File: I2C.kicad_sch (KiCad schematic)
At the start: 12 parts, among them U10 TCA9548AMRGER

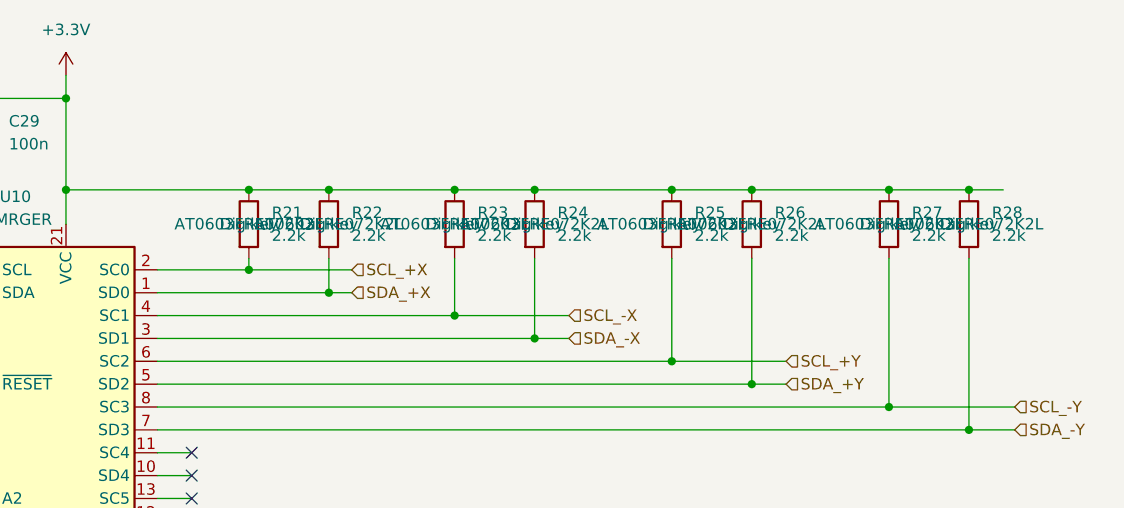
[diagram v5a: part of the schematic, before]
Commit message: Small schematic changes
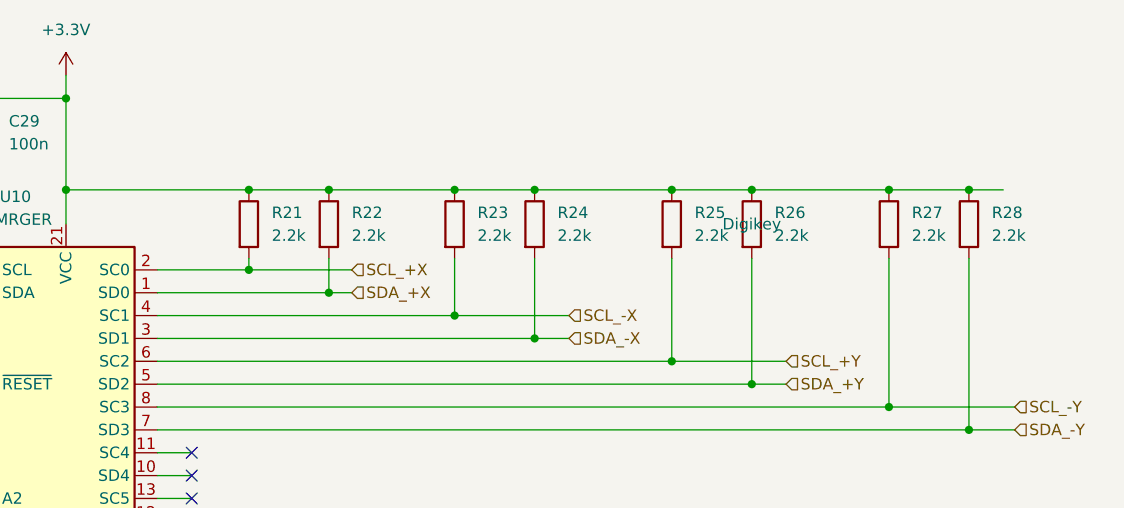
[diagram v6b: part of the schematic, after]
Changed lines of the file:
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@@
 					(size 1.27 1.27)
 				)
+				(hide yes)
 			)
 		)
@@
 					(size 1.27 1.27)
 				)
+				(hide yes)
 			)
 		)
@@
 					(size 1.27 1.27)
 				)
+				(hide yes)
 			)
 		)
@@
 					(size 1.27 1.27)
 				)
+				(hide yes)
 			)
 		)
@@
 					(size 1.27 1.27)
 				)
+				(hide yes)
 			)
 		)
@@
 					(size 1.27 1.27)
 				)
+				(hide yes)
 			)
 		)
@@
 					(size 1.27 1.27)
 				)
+				(hide yes)
 			)
 		)
@@
 					(size 1.27 1.27)
 				)
+				(hide yes)
 			)
 		)
@@
 					(size 1.27 1.27)
 				)
+				(hide yes)
 			)
 		)
@@
 					(size 1.27 1.27)
 				)
+				(hide yes)
 			)
 		)
@@
 					(size 1.27 1.27)
 				)
+				(hide yes)
 			)
 		)
@@
 					(size 1.27 1.27)
 				)
+				(hide yes)
 			)
 		)
@@
 					(size 1.27 1.27)
 				)
+				(hide yes)
 			)
 		)
@@
 					(size 1.27 1.27)
 				)
+				(hide yes)
 			)
 		)
@@
 					(size 1.27 1.27)
 				)
-			)
-		)
+				(hide yes)
+			)
+		)

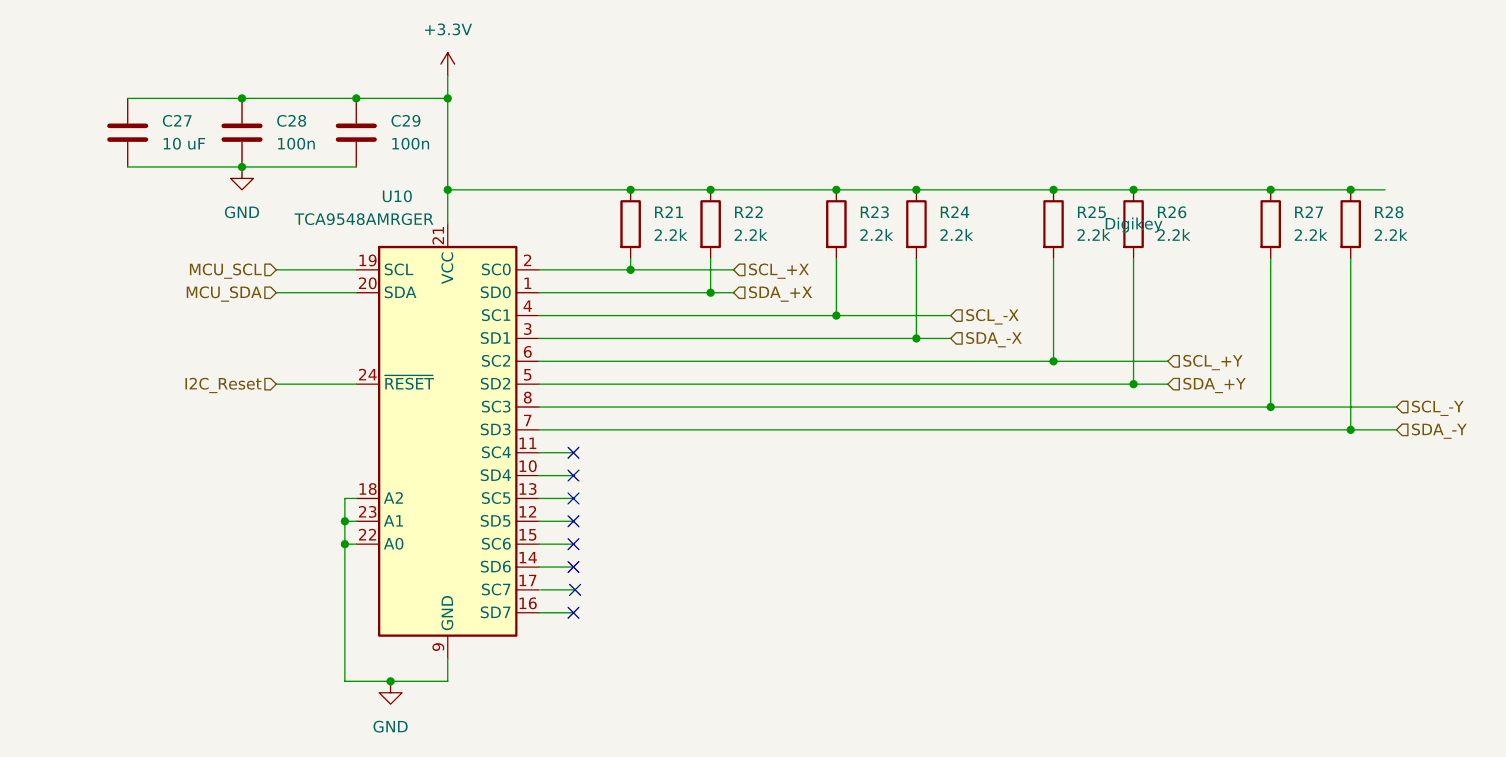
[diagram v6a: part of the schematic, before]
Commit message: Changed LTC 4412 to 4417, still kinks to work out
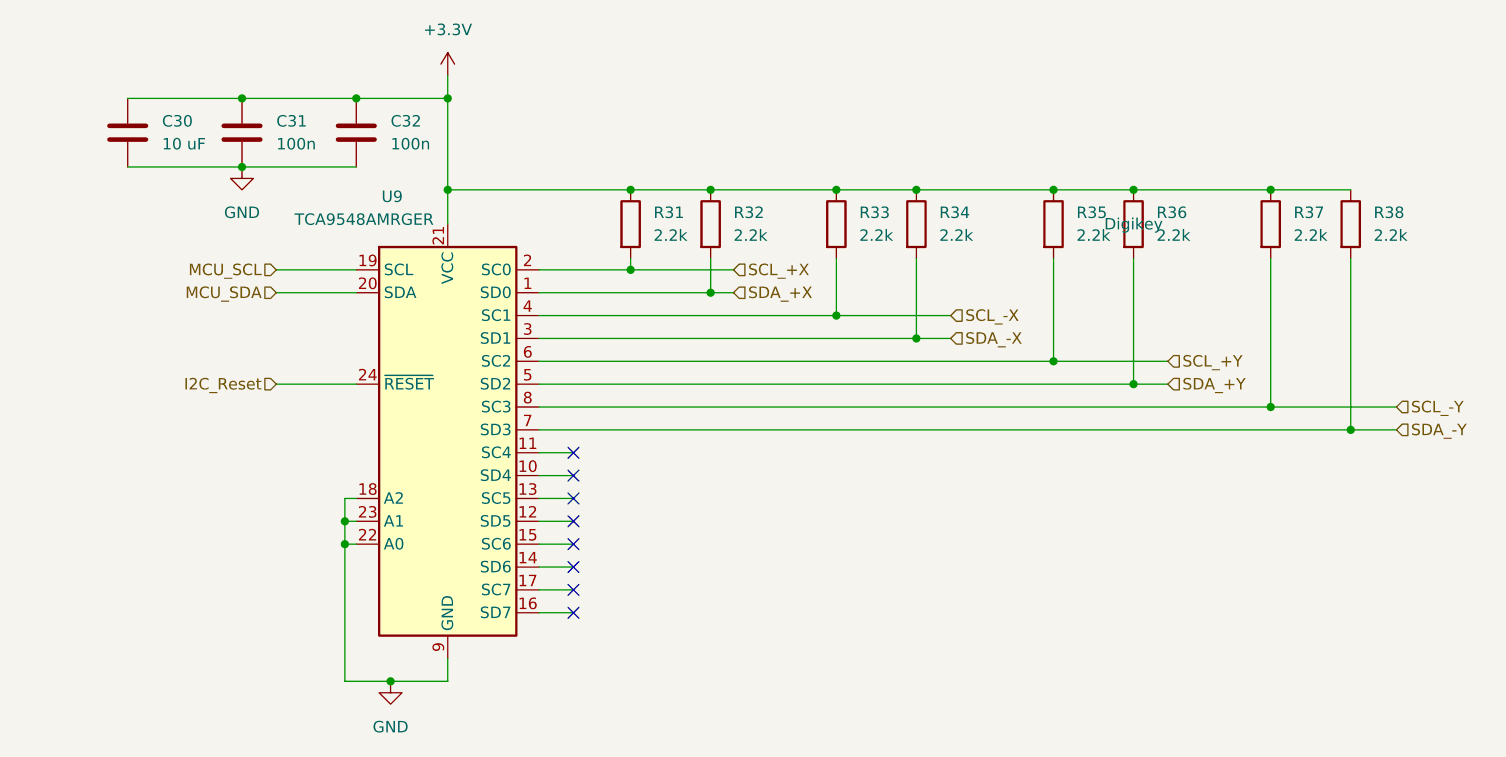
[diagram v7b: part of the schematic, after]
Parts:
- renumbered C27 to C30, C28 to C31, C29 to C32, R21 to R31, R22 to R32, R23 to R33, R24 to R34, R25 to R35, R26 to R36, R27 to R37, R28 to R38, U10 to U9
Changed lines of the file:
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@@
-	)
-	(junction
-		(at 229.87 62.23)
-		(diameter 0)
-		(color 0 0 0 0)
 	)
 	(junction
@@
 	)
 	(no_connect
-		(at 143.681 106.68)
-	)
-	(wire
-		(pts
-			(xy 139.871 106.68) (xy 143.681 106.68)
+		(at 143.51 106.68)
+	)
+	(wire
+		(pts
+			(xy 139.7 106.68) (xy 143.51 106.68)
 		)
 		(stroke
@@
 		(pts
 			(xy 181.61 69.85) (xy 181.61 78.74)
-		)
-		(stroke
-			(width 0)
-			(type default)
-		)
-	)
-	(wire
-		(pts
-			(xy 229.87 62.23) (xy 233.68 62.23)
 		)
 		(stroke
@@
 		(dnp no)
 		(fields_autoplaced yes)
-		(property "Reference" "R26"
+		(property "Reference" "R36"
 			(at 208.28 64.7699 0)
 			(effects
@@
 			(project "EPS_mppt_board"
 				(path "/8f246f89-1ec7-4136-9977-839b50e116ed/0b35a7b5-b504-4fbf-9bb2-d6dcd13c2d56"
-					(reference "R26")
+					(reference "R36")
 					(unit 1)
 				)
@@
 		(dnp no)
 		(fields_autoplaced yes)
-		(property "Reference" "C28"
+		(property "Reference" "C31"
 			(at 110.49 54.6099 0)
 			(effects
@@
 			(project "EPS_mppt_board"
 				(path "/8f246f89-1ec7-4136-9977-839b50e116ed/0b35a7b5-b504-4fbf-9bb2-d6dcd13c2d56"
-					(reference "C28")
+					(reference "C31")
 					(unit 1)
 				)
@@
 		(dnp no)
 		(fields_autoplaced yes)
-		(property "Reference" "C27"
+		(property "Reference" "C30"
 			(at 97.79 54.6099 0)
 			(effects
@@
 			(project "EPS_mppt_board"
 				(path "/8f246f89-1ec7-4136-9977-839b50e116ed/0b35a7b5-b504-4fbf-9bb2-d6dcd13c2d56"
-					(reference "C27")
+					(reference "C30")
 					(unit 1)
 				)
@@
 		(dnp no)
 		(fields_autoplaced yes)
-		(property "Reference" "#PWR057"
+		(property "Reference" "#PWR064"
 			(at 123.19 123.19 0)
 			(effects
@@
 			(project ""
 				(path "/8f246f89-1ec7-4136-9977-839b50e116ed/0b35a7b5-b504-4fbf-9bb2-d6dcd13c2d56"
-					(reference "#PWR057")
+					(reference "#PWR064")
 					(unit 1)
 				)
@@
 		(dnp no)
 		(fields_autoplaced yes)
-		(property "Reference" "R22"
+		(property "Reference" "R32"
 			(at 161.29 64.7699 0)
 			(effects
@@
 			(project "EPS_mppt_board"
 				(path "/8f246f89-1ec7-4136-9977-839b50e116ed/0b35a7b5-b504-4fbf-9bb2-d6dcd13c2d56"
-					(reference "R22")
+					(reference "R32")
 					(unit 1)
 				)
@@
 		(dnp no)
 		(fields_autoplaced yes)
-		(property "Reference" "R23"
+		(property "Reference" "R33"
 			(at 175.26 64.7699 0)
 			(effects
@@
 			(project "EPS_mppt_board"
 				(path "/8f246f89-1ec7-4136-9977-839b50e116ed/0b35a7b5-b504-4fbf-9bb2-d6dcd13c2d56"
-					(reference "R23")
+					(reference "R33")
 					(unit 1)
 				)
@@
 		(dnp no)
 		(fields_autoplaced yes)
-		(property "Reference" "#PWR056"
+		(property "Reference" "#PWR063"
 			(at 106.68 66.04 0)
 			(effects
@@
 			(project "EPS_mppt_board"
 				(path "/8f246f89-1ec7-4136-9977-839b50e116ed/0b35a7b5-b504-4fbf-9bb2-d6dcd13c2d56"
-					(reference "#PWR056")
+					(reference "#PWR063")
 					(unit 1)
 				)
@@
 		(dnp no)
 		(fields_autoplaced yes)
-		(property "Reference" "R21"
+		(property "Reference" "R31"
 			(at 152.4 64.7699 0)
 			(effects
@@
 			(project ""
 				(path "/8f246f89-1ec7-4136-9977-839b50e116ed/0b35a7b5-b504-4fbf-9bb2-d6dcd13c2d56"
-					(reference "R21")
+					(reference "R31")
 					(unit 1)
 				)
@@
 		(dnp no)
 		(fields_autoplaced yes)
-		(property "Reference" "R24"
+		(property "Reference" "R34"
 			(at 184.15 64.7699 0)
 			(effects
@@
 			(project "EPS_mppt_board"
 				(path "/8f246f89-1ec7-4136-9977-839b50e116ed/0b35a7b5-b504-4fbf-9bb2-d6dcd13c2d56"
-					(reference "R24")
+					(reference "R34")
 					(unit 1)
 				)
@@
 		(on_board yes)
 		(dnp no)
-		(property "Reference" "U10"
+		(property "Reference" "U9"
 			(at 122.174 62.992 0)
 			(effects
@@
 			(project ""
 				(path "/8f246f89-1ec7-4136-9977-839b50e116ed/0b35a7b5-b504-4fbf-9bb2-d6dcd13c2d56"
-					(reference "U10")
+					(reference "U9")
 					(unit 1)
 				)
@@
 		(dnp no)
 		(fields_autoplaced yes)
-		(property "Reference" "R27"
+		(property "Reference" "R37"
 			(at 223.52 64.7699 0)
 			(effects
@@
 			(project "EPS_mppt_board"
 				(path "/8f246f89-1ec7-4136-9977-839b50e116ed/0b35a7b5-b504-4fbf-9bb2-d6dcd13c2d56"
-					(reference "R27")
+					(reference "R37")
 					(unit 1)
 				)
@@
 		(dnp no)
 		(fields_autoplaced yes)
-		(property "Reference" "R28"
+		(property "Reference" "R38"
 			(at 232.41 64.7699 0)
 			(effects
@@
 			(project "EPS_mppt_board"
 				(path "/8f246f89-1ec7-4136-9977-839b50e116ed/0b35a7b5-b504-4fbf-9bb2-d6dcd13c2d56"
-					(reference "R28")
+					(reference "R38")
 					(unit 1)
 				)
@@
 		(dnp no)
 		(fields_autoplaced yes)
-		(property "Reference" "C29"
+		(property "Reference" "C32"
 			(at 123.19 54.6099 0)
 			(effects
@@
 			(project ""
 				(path "/8f246f89-1ec7-4136-9977-839b50e116ed/0b35a7b5-b504-4fbf-9bb2-d6dcd13c2d56"
-					(reference "C29")
+					(reference "C32")
 					(unit 1)
 				)
@@
 		(dnp no)
 		(fields_autoplaced yes)
-		(property "Reference" "#PWR055"
+		(property "Reference" "#PWR065"
 			(at 129.54 53.34 0)
 			(effects
@@
 			(project ""
 				(path "/8f246f89-1ec7-4136-9977-839b50e116ed/0b35a7b5-b504-4fbf-9bb2-d6dcd13c2d56"
-					(reference "#PWR055")
+					(reference "#PWR065")
 					(unit 1)
 				)
@@
 		(dnp no)
 		(fields_autoplaced yes)
-		(property "Reference" "R25"
+		(property "Reference" "R35"
 			(at 199.39 64.7699 0)
 			(effects
@@
 			(project "EPS_mppt_board"
 				(path "/8f246f89-1ec7-4136-9977-839b50e116ed/0b35a7b5-b504-4fbf-9bb2-d6dcd13c2d56"
-					(reference "R25")
+					(reference "R35")
 					(unit 1)
 				)
